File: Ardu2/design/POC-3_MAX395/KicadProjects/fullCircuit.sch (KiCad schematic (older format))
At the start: 125 parts, among them P1 CONN_01X02, P7 CONN_01X15, U1 Pyboard, U10 MAX395, U11 MAX395, U12 MAX395, U13 MAX395, U14 MAX395, U15 MAX395, U16 MAX395, U17 MAX395, U18 MAX395, U2 LM2596, U3 LM2596, U4 Vactrol, U5 MAX395, U6 MAX395, U7 MAX395, U8 MAX395, U9 MAX395

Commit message: minor improvements to PCB
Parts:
- removed L3: 1mH, 330L:Inductor, symbol INDUCTOR
- R1: value 220 -> 1K
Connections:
- net MIn- is gone; now on net GND: C10.2, C11.2, C12.1, C13.1, C14.1, P7.1 (P1), P7.10 (P10), P7.6 (P6), P7.7 (P7), P7.8 (P8), P7.9 (P9), R15.1, R6.1, U10.13 (COM4), U13.20 (NO7), U4.3 (Rl), U5.9 (NO2), U7.14 (NO4), U7.15 (COM5)
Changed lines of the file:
@@
 Sheet 1 1
 Title "ArduGuitar Full Circuit MAX395"
-Date "Sun 31 May 2015"
-Rev "1.3"
+Date "Tue 09 Jun 2015"
+Rev "1.4"
 Comp "www.arduguitar.org"
-Comment1 ""
+Comment1 "removed ground separation inductor"
 Comment2 ""
 Comment3 ""
@@
 P 1550 1450
 F 0 "R1" V 1630 1450 50  0000 C CNN
-F 1 "220" V 1550 1450 50  0000 C CNN
+F 1 "1K" V 1550 1450 50  0000 C CNN
 F 2 "Resistors_ThroughHole:Resistor_Horizontal_RM10mm" V 1480 1450 30  0001 C CNN
 F 3 "" H 1550 1450 30  0000 C CNN
@@
 	1    2100 5900
 	1    0    0    -1
-$EndComp
-$Comp
-L INDUCTOR L3
-U 1 1 55629072
-P 5350 1400
-F 0 "L3" V 5300 1400 50  0000 C CNN
-F 1 "1mH" V 5450 1400 50  0000 C CNN
-F 2 "330L:Inductor" H 5350 1400 60  0001 C CNN
-F 3 "" H 5350 1400 60  0000 C CNN
-	1    5350 1400
-	0    -1   -1   0
 $EndComp
 $Comp
@@
 L GND #PWR016
 U 1 1 5564E4CD
-P 4950 1400
-F 0 "#PWR016" H 4950 1150 50  0001 C CNN
-F 1 "GND" H 4950 1250 50  0000 C CNN
-F 2 "" H 4950 1400 60  0000 C CNN
-F 3 "" H 4950 1400 60  0000 C CNN
-	1    4950 1400
-	0    1    1    0
+P 5650 1450
+F 0 "#PWR016" H 5650 1200 50  0001 C CNN
+F 1 "GND" H 5650 1300 50  0000 C CNN
+F 2 "" H 5650 1450 60  0000 C CNN
+F 3 "" H 5650 1450 60  0000 C CNN
+	1    5650 1450
+	1    0    0    -1
 $EndComp
 Text Label 5250 1000 3    60   ~ 0
@@
 Connection ~ 10300 7400
 Connection ~ 1550 1700
-Wire Wire Line
-	4950 1400 5050 1400
 Connection ~ 6150 7400
 Wire Wire Line
@@
 Connection ~ 5950 1000
 Wire Wire Line
-	5650 1400 5650 1000
+	5650 1000 5650 1450
 Text Label 750  3600 0    60   ~ 0
 ShuntControl

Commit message: Updates after mockup of PCB
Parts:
- C2, C3: footprint Capacitors_ThroughHole:C_Radial_D10_L16_P5 -> Capacitors_ThroughHole:C_Radial_D8_L11.5_P3.5
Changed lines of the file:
@@
 F 0 "C3" H 4125 7300 50  0000 L CNN
 F 1 "220µF" H 4125 7100 50  0000 L CNN
-F 2 "Capacitors_ThroughHole:C_Radial_D10_L16_P5" H 4138 7050 30  0001 C CNN
+F 2 "Capacitors_ThroughHole:C_Radial_D8_L11.5_P3.5" H 4138 7050 30  0001 C CNN
 F 3 "" H 4100 7200 60  0000 C CNN
 	1    4100 7200
@@
 F 0 "C2" H 1925 8750 50  0000 L CNN
 F 1 "220µF" H 1925 8550 50  0000 L CNN
-F 2 "Capacitors_ThroughHole:C_Radial_D10_L16_P5" H 1938 8500 30  0001 C CNN
+F 2 "Capacitors_ThroughHole:C_Radial_D8_L11.5_P3.5" H 1938 8500 30  0001 C CNN
 F 3 "" H 1900 8650 60  0000 C CNN
 	1    1900 8650

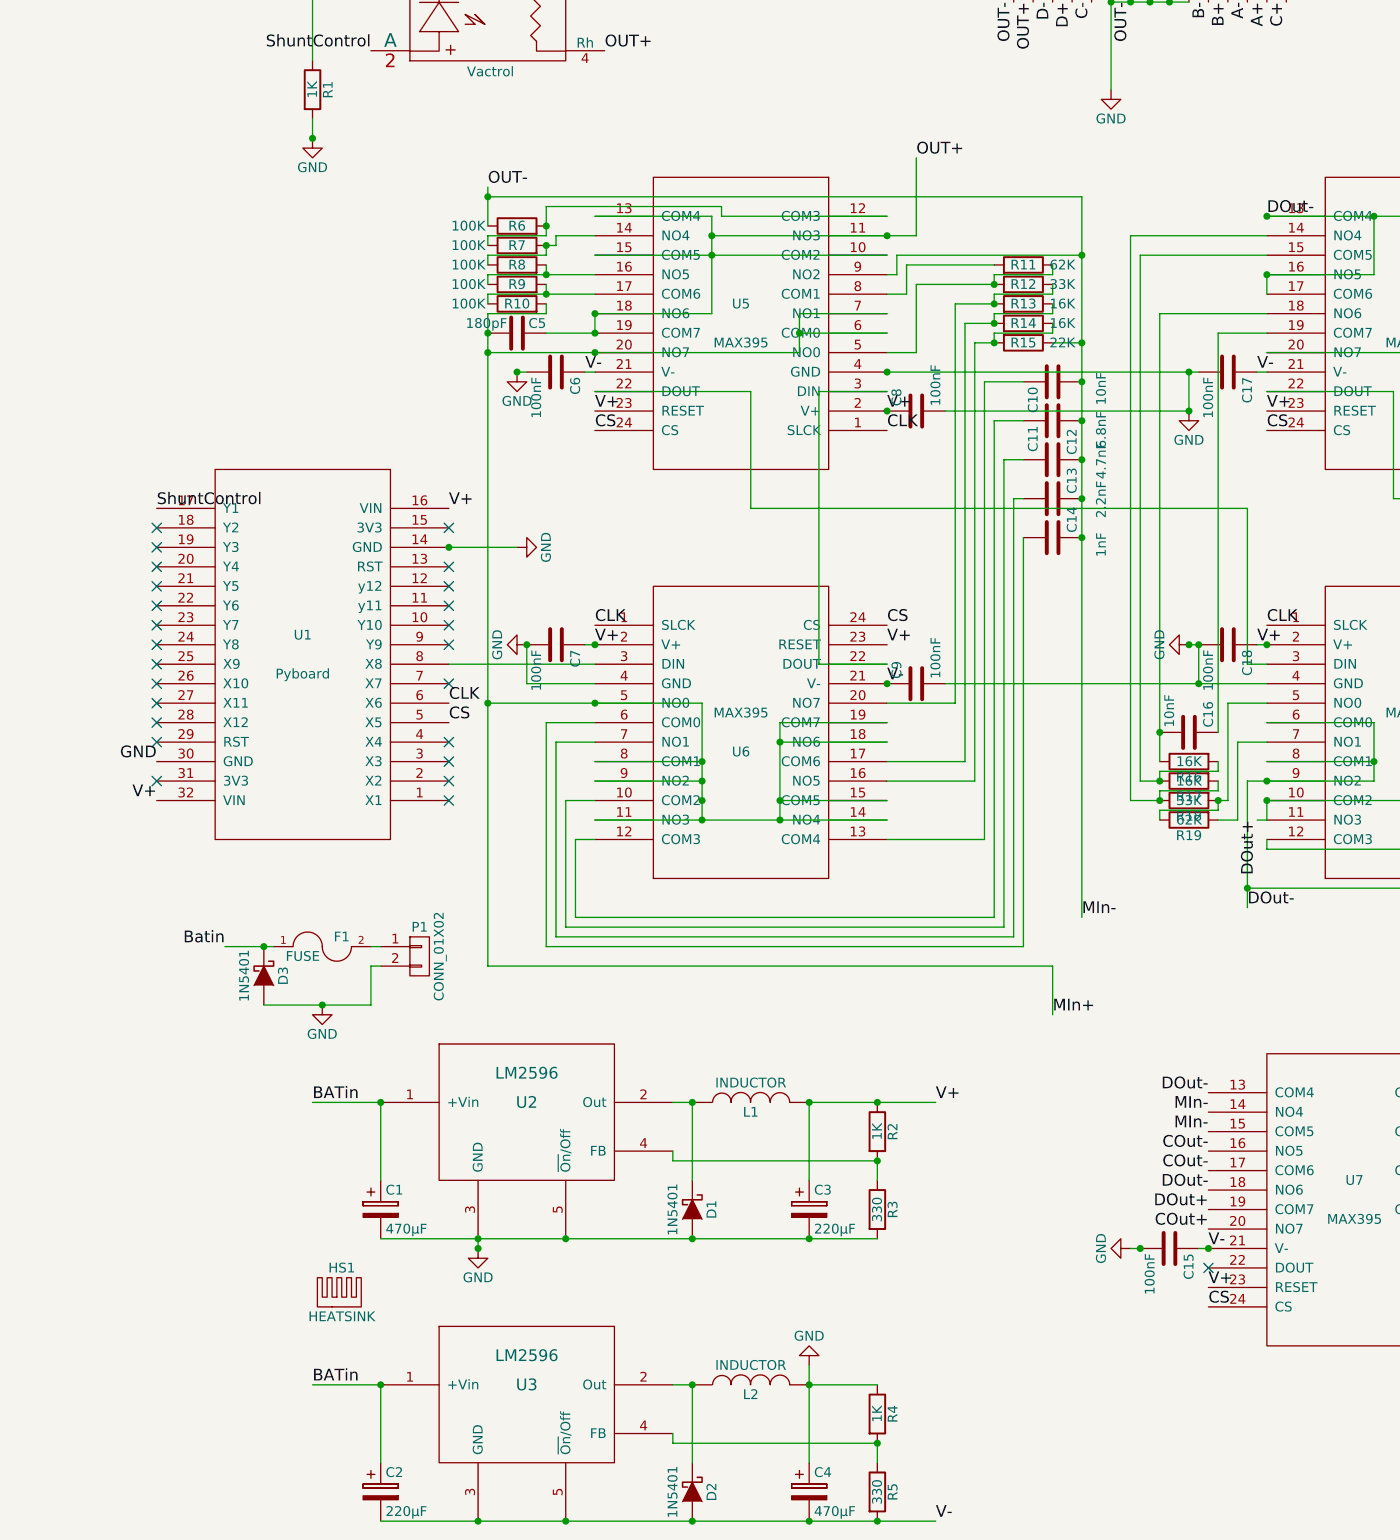
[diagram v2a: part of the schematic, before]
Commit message: updates to circuit with SENSEI
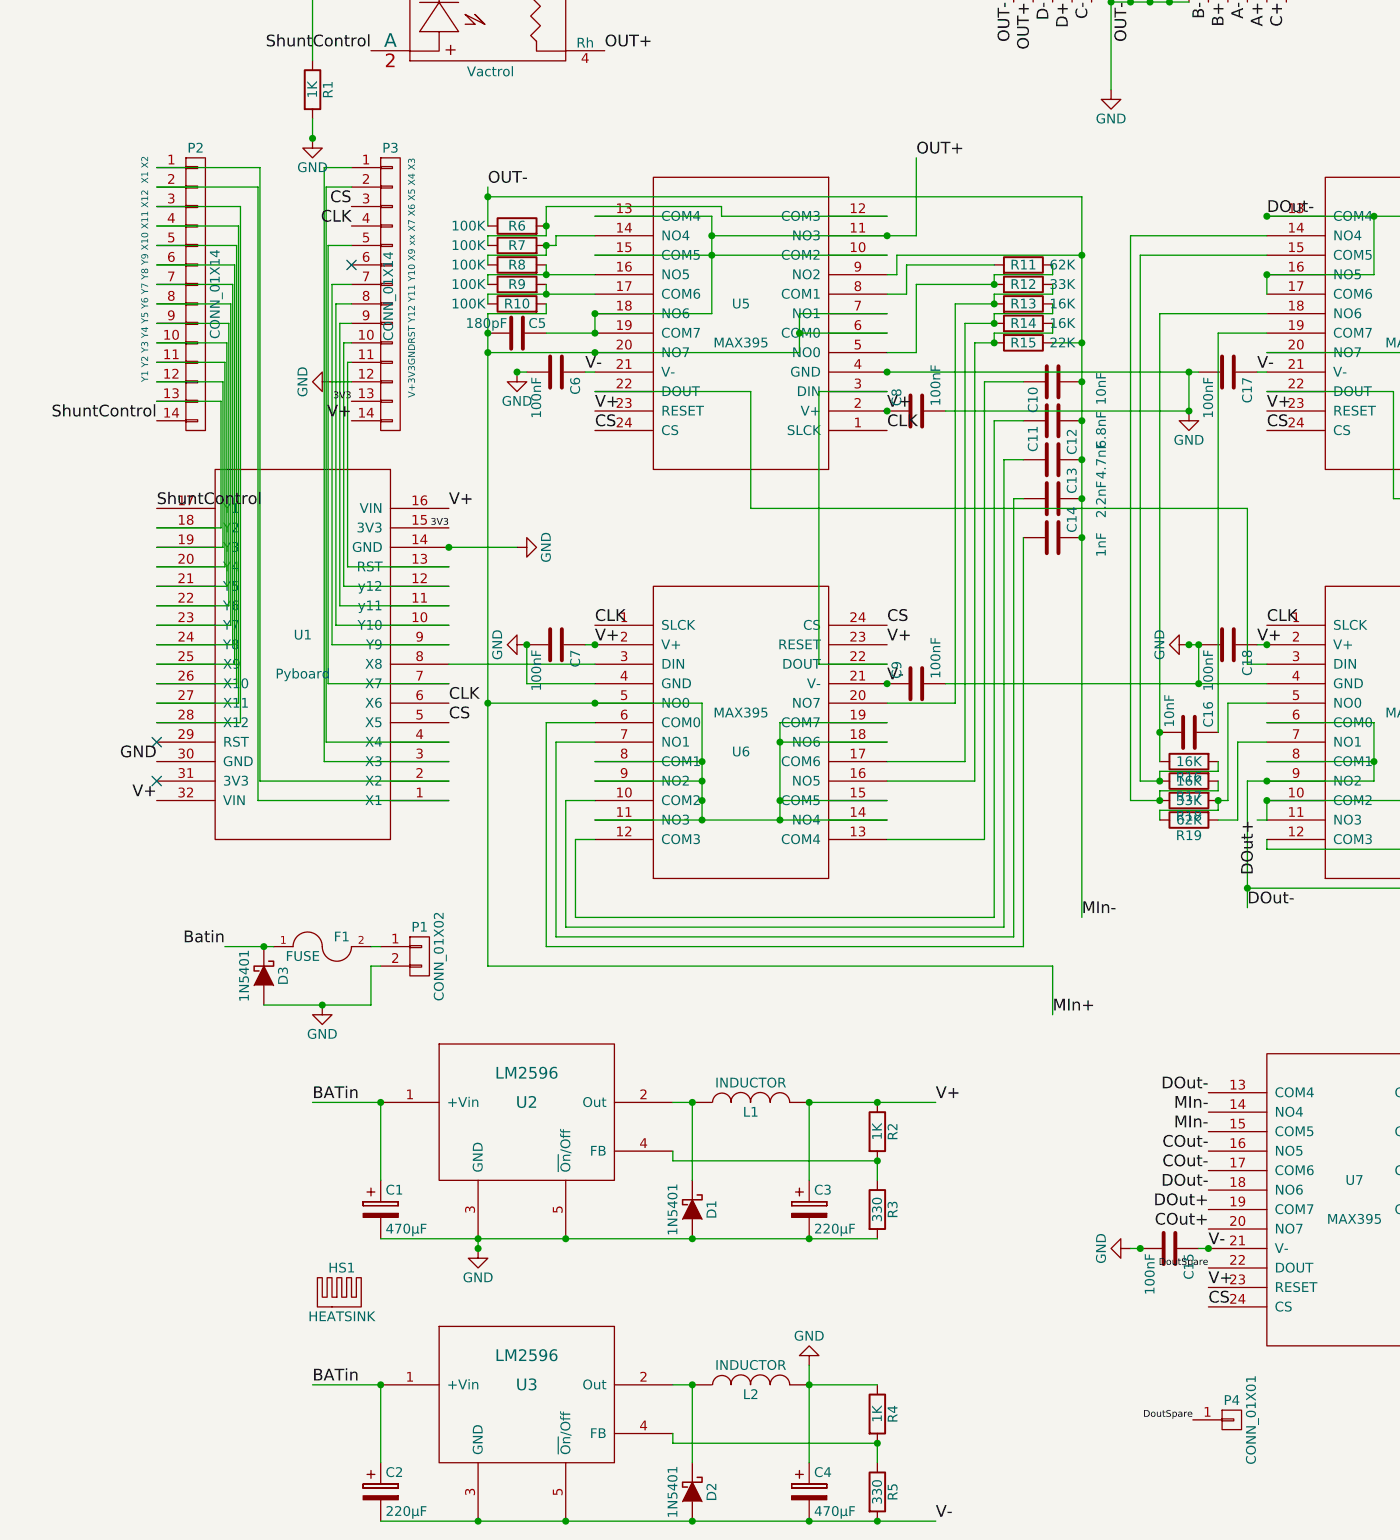
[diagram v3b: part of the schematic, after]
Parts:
- added P2, P3: CONN_01X14, Pin_Headers:Pin_Header_Straight_1x14, symbol CONN_01X14
- added P4: CONN_01X01, Pin_Headers:Pin_Header_Straight_1x01, symbol CONN_01X01
- U10, U11, U12, U13, U14, U15, U16, U17, U18, U5, U6, U7, U8, U9: footprint Housings_DIP:DIP-24__300 -> 330L:DIP-24__300_pads_70_10
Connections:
- net CLK: now also P3.4 (P4)
- net CS: now also P3.3 (P3)
- net GND: now also P3.12 (P12)
- net ShuntControl: now also P2.14 (P14)
- net V+: now also P3.14 (P14)
- net DoutSpare: now reaches U7.22 (DOUT)
- net DoutSpare: now also P4.1 (P1)
- net at U1.1 (X1): now also P2.2 (P2)
- net at U1.10 (Y10): now also P3.8 (P8)
- net at U1.11 (y11): now also P3.9 (P9)
- net at U1.12 (y12): now also P3.10 (P10)
- net at U1.13 (RST): now also P3.11 (P11)
- net 3V3: now reaches U1.15 (3V3)
- net 3V3: now also P3.13 (P13)
- net at U1.18 (Y2): now also P2.13 (P13)
- net at U1.19 (Y3): now also P2.12 (P12)
- net at U1.2 (X2): now also P2.1 (P1)
- net at U1.20 (Y4): now also P2.11 (P11)
- net at U1.21 (Y5): now also P2.10 (P10)
- net at U1.22 (Y6): now also P2.9 (P9)
- net at U1.23 (Y7): now also P2.8 (P8)
- net at U1.24 (Y8): now also P2.7 (P7)
- net at U1.25 (X9): now also P2.6 (P6)
- net at U1.26 (X10): now also P2.5 (P5)
- net at U1.27 (X11): now also P2.4 (P4)
- net at U1.28 (X12): now also P2.3 (P3)
- net at U1.3 (X3): now also P3.1 (P1)
- net at U1.4 (X4): now also P3.2 (P2)
- net at U1.7 (X7): now also P3.5 (P5)
- net at U1.9 (Y9): now also P3.7 (P7)
- no-connect marks 25 -> 3
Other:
- note added: "V+3V3GNDRST Y12 Y11 Y10 X9 xx X7 X6 X5 X4 X3"
- note added: "Y1 Y2 Y3 Y4 Y5 Y6 Y7 Y8 Y9 X10 X11 X12 X1 X2"

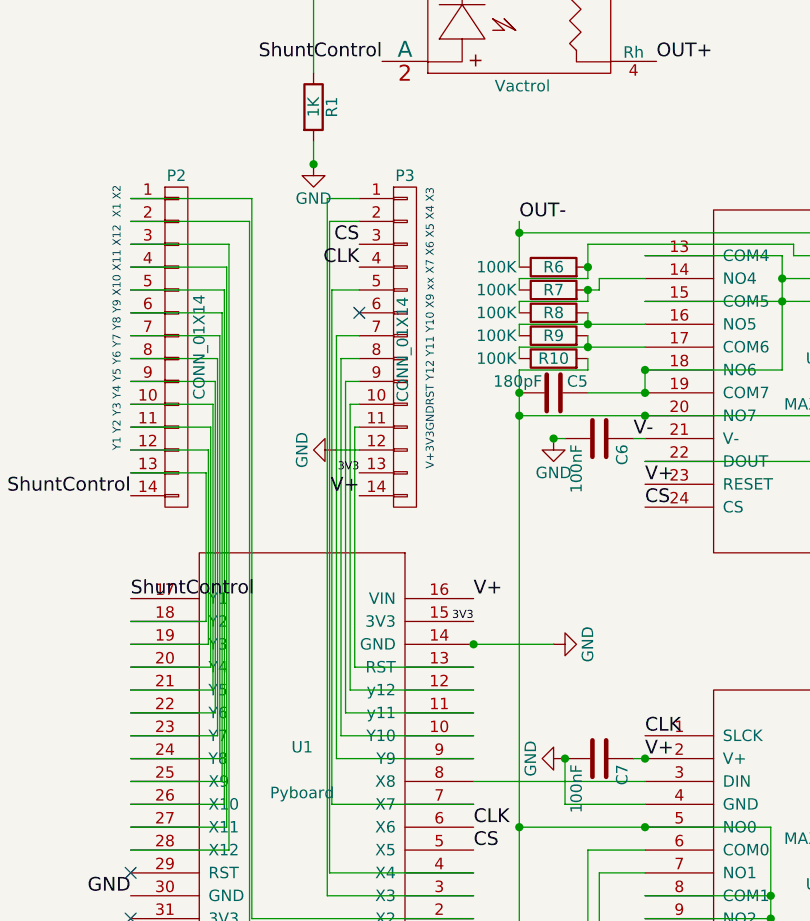
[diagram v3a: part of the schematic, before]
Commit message: updates to the headers conf on pcb
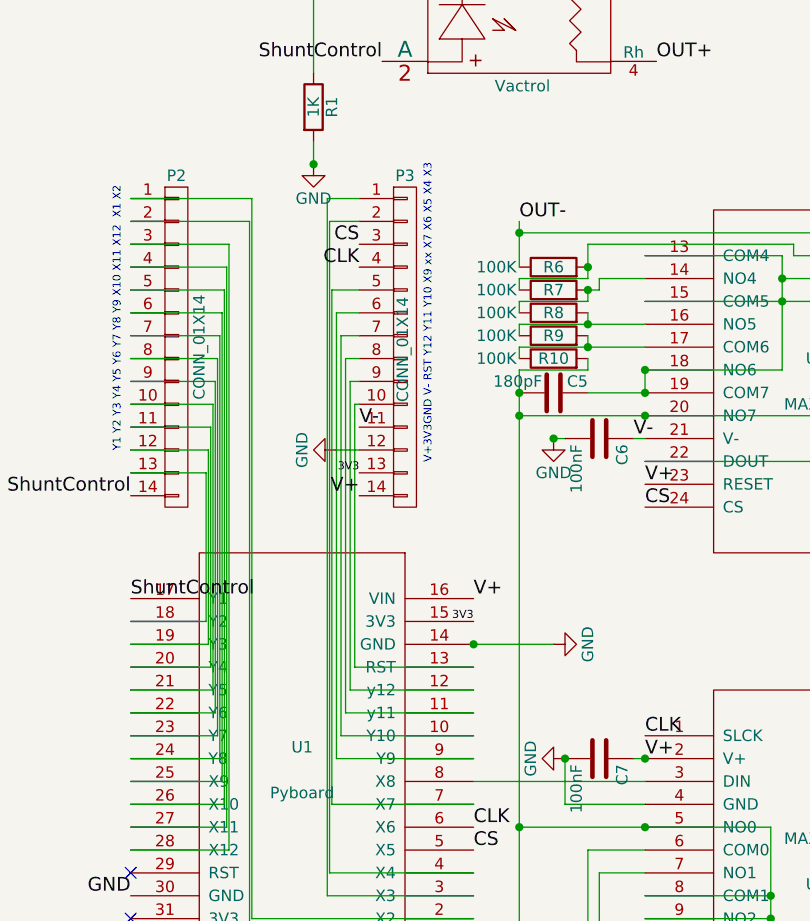
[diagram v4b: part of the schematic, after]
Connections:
- net V-: now also P3.11 (P11)
- net at U1.10 (Y10): now also P3.7 (P7); no longer P3.8 (P8)
- net at U1.11 (y11): now also P3.8 (P8); no longer P3.9 (P9)
- net at U1.12 (y12): now also P3.9 (P9); no longer P3.10 (P10)
- net at U1.13 (RST): now also P3.10 (P10); no longer P3.11 (P11)
- net at U1.9 (Y9): now also P3.6 (P6); no longer P3.7 (P7)
- no-connect marks 3 -> 2
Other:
- note added: "V+3V3GND V- RST Y12 Y11 Y10 X9 xx X7 X6 X5 X4 X3"
- note removed: "V+3V3GNDRST Y12 Y11 Y10 X9 xx X7 X6 X5 X4 X3"

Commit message: updates to the pcb layout this corresponds to the working prototype PCB
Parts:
- P7: footprint w_conn_pc:DB_15F-VGA -> w_conn_pc:DB_15F-VGA_00_BOB
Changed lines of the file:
@@
 Sheet 1 1
 Title "ArduGuitar Full Circuit MAX395"
-Date "2015-06-18"
-Rev "1.6"
+Date "2015-11-02"
+Rev "1.7"
 Comp "www.arduguitar.org"
 Comment1 "update after review,"
 Comment2 "added V+/V- to headers"
-Comment3 ""
+Comment3 "changed VGA Connector footprint"
 Comment4 ""
 $EndDescr
@@
 F 0 "P7" H 5850 1600 50  0000 C CNN
 F 1 "CONN_01X15" V 5950 800 50  0000 C CNN
-F 2 "w_conn_pc:DB_15F-VGA" H 5850 800 60  0001 C CNN
+F 2 "w_conn_pc:DB_15F-VGA_00_BOB" H 5850 800 60  0001 C CNN
 F 3 "" H 5850 800 60  0000 C CNN
 	1    5850 800

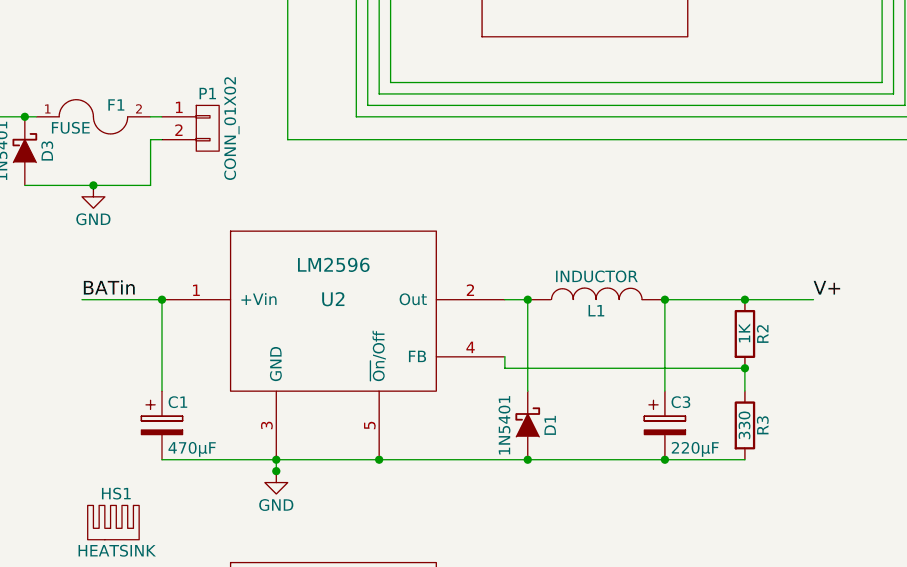
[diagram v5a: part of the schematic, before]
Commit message: update to circuit for schottkey protection diode
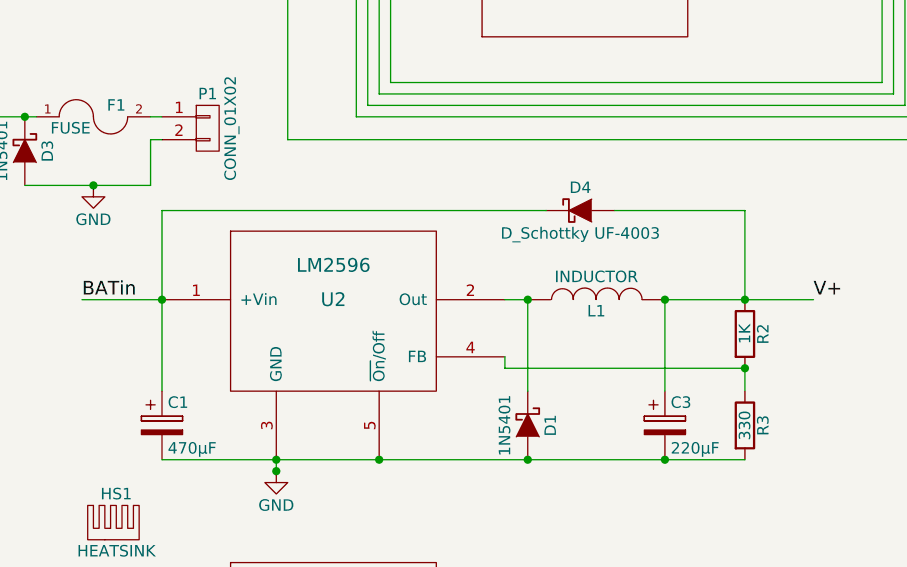
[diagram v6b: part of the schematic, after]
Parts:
- added D4: D_Schottky UF-4003, Diodes_ThroughHole:Diode_DO-41_SOD81_Horizontal_RM10, symbol D_Schottky
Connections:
- net BATin: now also D4.1 (K)
- net V+: now also D4.2 (A)
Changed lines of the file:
@@
 Sheet 1 1
 Title "ArduGuitar Full Circuit MAX395"
-Date "2015-11-02"
-Rev "1.7"
+Date "2015-11-04"
+Rev "1.8"
 Comp "www.arduguitar.org"
 Comment1 "update after review,"
 Comment2 "added V+/V- to headers"
 Comment3 "changed VGA Connector footprint"
-Comment4 ""
+Comment4 "addec schottkey to prevent LM2596 latch-up"
 $EndDescr
 $Comp
@@
 	1550 6650 1900 6650
 Wire Wire Line
-	1900 6650 1900 7050
+	1900 6260 1900 7050
 Wire Wire Line
 	18750 4600 18750 4800
@@
 Text Label 1750 2850 0    60   ~ 0
 V-
+$Comp
+L D_Schottky D4
+U 1 1 563A18BC
+P 3730 6260
+F 0 "D4" H 3730 6360 50  0000 C CNN
+F 1 "D_Schottky UF-4003" H 3730 6160 50  0000 C CNN
+F 2 "Diodes_ThroughHole:Diode_DO-41_SOD81_Horizontal_RM10" H 3730 6260 60  0001 C CNN
+F 3 "" H 3730 6260 60  0000 C CNN
+	1    3730 6260
+	1    0    0    -1
+$EndComp
+Wire Wire Line
+	3880 6260 4450 6260
+Wire Wire Line
+	4450 6260 4450 6650
+Wire Wire Line
+	3580 6260 1900 6260
 $EndSCHEMATC
